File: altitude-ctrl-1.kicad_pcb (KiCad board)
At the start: 2 copper layers, 90 x 90 mm, 93 parts, among them J1 Conn_01x02, J10 Conn_01x02, J11 Conn_01x04, J2 Conn_01x02, J3 Conn_01x05, J4 TC2030, J5 Conn_01x04_Pin, J6 Conn_01x02, J7 Conn_01x05, J8 Conn_01x05, J9 Conn_01x02, SW1 SW_Push, SW2 SW_SPST, SW3 SW_Push, SW4 SW_SPST, SW5 SW_Push, U1 HT753-1, U2 ULN2003A, U3 LM73100, U4 LM73100, U5 MAX6675, U6 STM32F103C8Tx, U7 SN65HVD230, Y1 8M

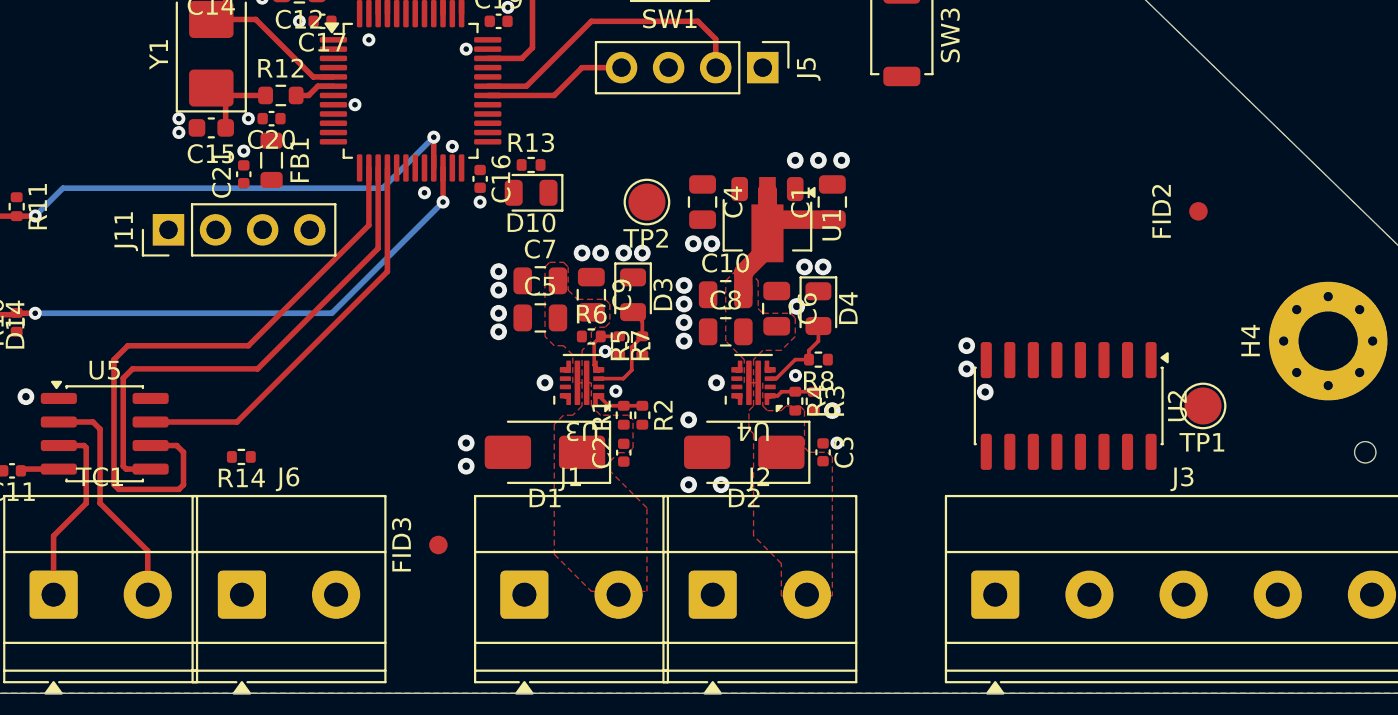
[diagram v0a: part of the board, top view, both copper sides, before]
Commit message: pcb: add relay driver routing
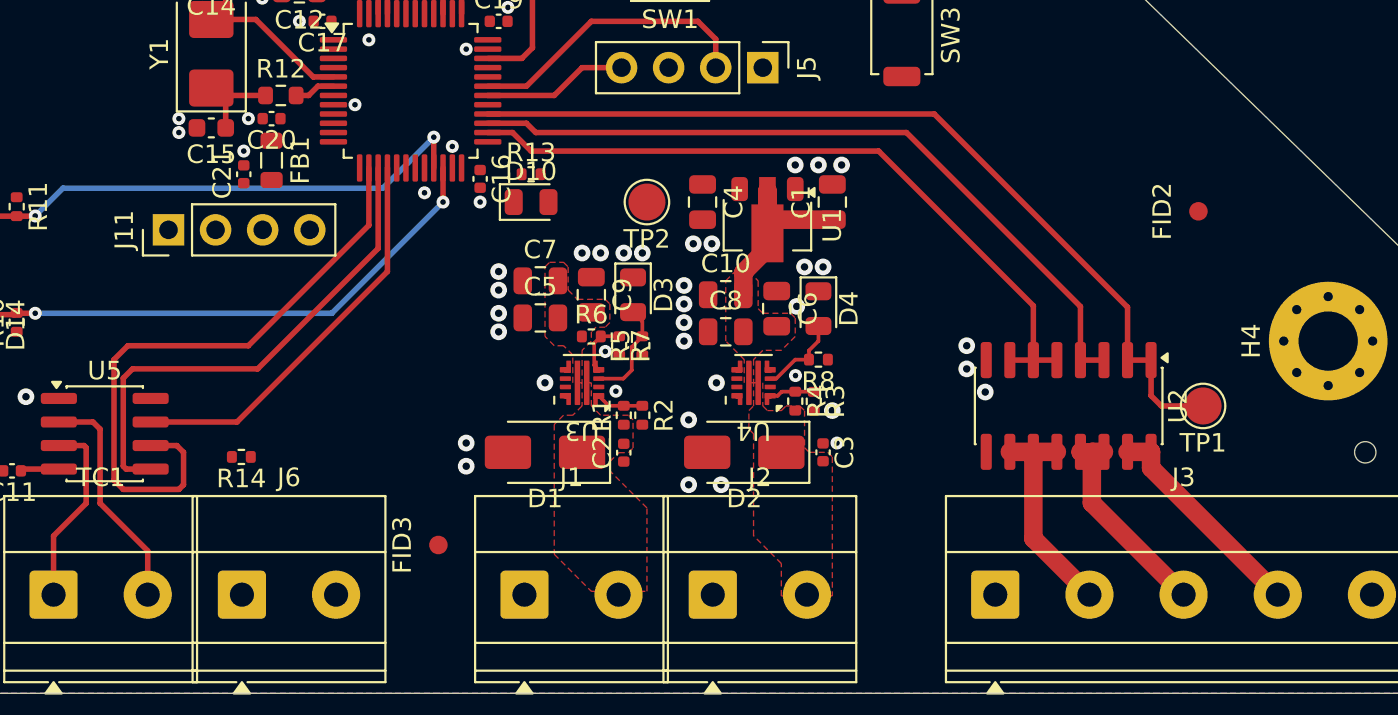
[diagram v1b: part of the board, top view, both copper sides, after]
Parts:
- moved D10 0.50 mm to (171.0, 92.5), turned to 0 degrees
- moved R13 0.50 mm to (171.0, 91.0)
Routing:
- net /PUMP: track 0.00 -> 47.9 mm
- net /RL1: track 0.00 -> 40.2 mm
- net /RL2: track 0.00 -> 38.8 mm
- net Net-(J3-Pin_4): track 0.00 -> 11.8 mm
- net Net-(J3-Pin_2): track 0.00 -> 11.5 mm
- net Net-(J3-Pin_3): track 0.00 -> 11.0 mm

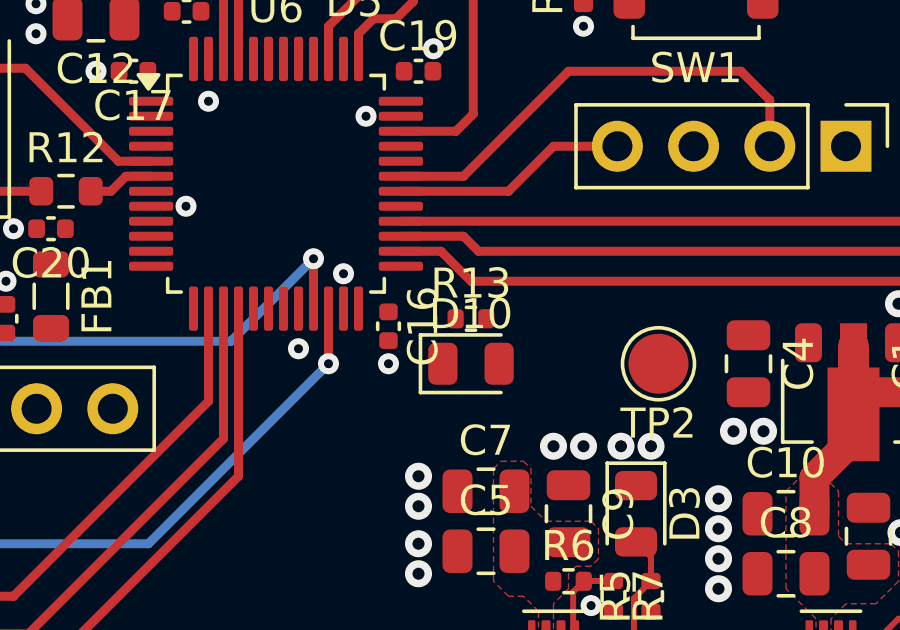
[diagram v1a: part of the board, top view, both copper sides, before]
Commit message: pcb: add can status led routing
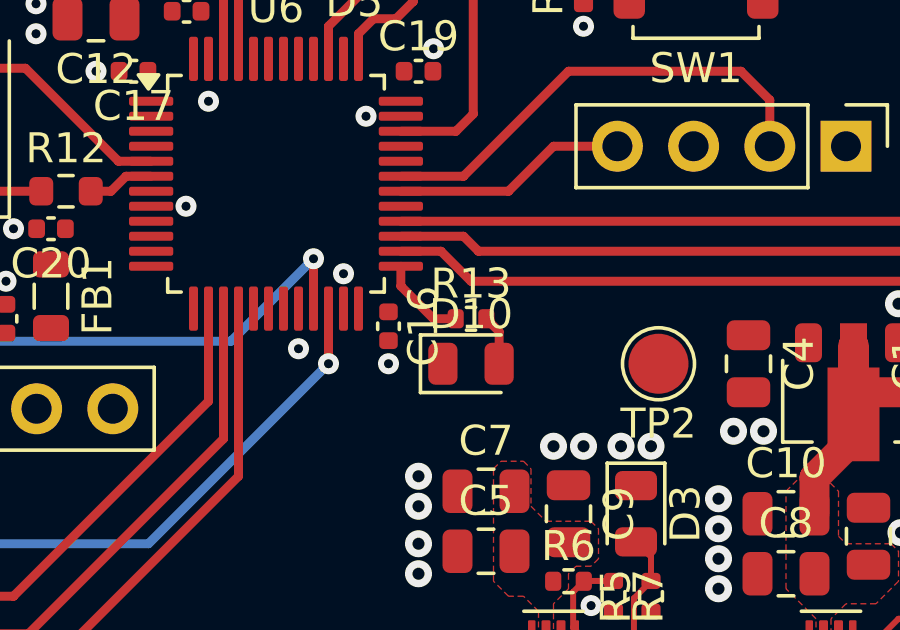
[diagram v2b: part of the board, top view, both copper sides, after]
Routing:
- net Net-(U6-PB12): track 0.00 -> 2.94 mm
- net Net-(D10-A): track 0.00 -> 1.68 mm
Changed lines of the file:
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@@
+	)
+	(segment
+		(start 171.9375 91.4275)
+		(end 171.51 91)
+		(width 0.3)
+		(layer "F.Cu")
+		(net "Net-(D10-A)")
+	)
+	(segment
+		(start 171.9375 92.5)
+		(end 171.9375 91.4275)
+		(width 0.3)
+		(layer "F.Cu")
+		(net "Net-(D10-A)")
 	)
 	(segment
@@
 		(net "Net-(TC1-+)")
 	)
+	(segment
+		(start 168.6625 89.9125)
+		(end 169.75 91)
+		(width 0.3)
+		(layer "F.Cu")
+		(net "Net-(U6-PB12)")
+	)
+	(segment
+		(start 169.75 91)
+		(end 170.49 91)
+		(width 0.3)
+		(layer "F.Cu")
+		(net "Net-(U6-PB12)")
+	)
+	(segment
+		(start 168.6625 89.25)
+		(end 168.6625 89.9125)
+		(width 0.3)
+		(layer "F.Cu")
+		(net "Net-(U6-PB12)")
+	)
 	(zone

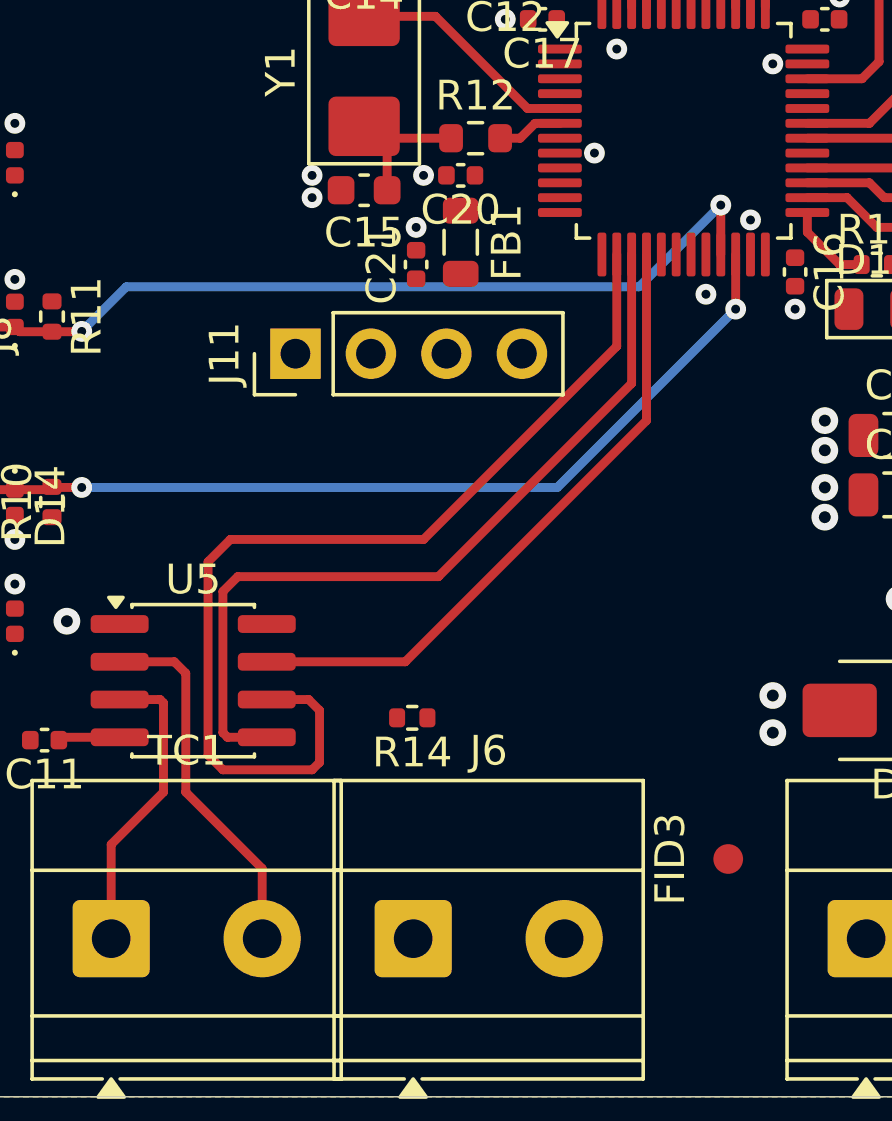
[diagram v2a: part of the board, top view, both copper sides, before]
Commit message: pcb: add gpio routing
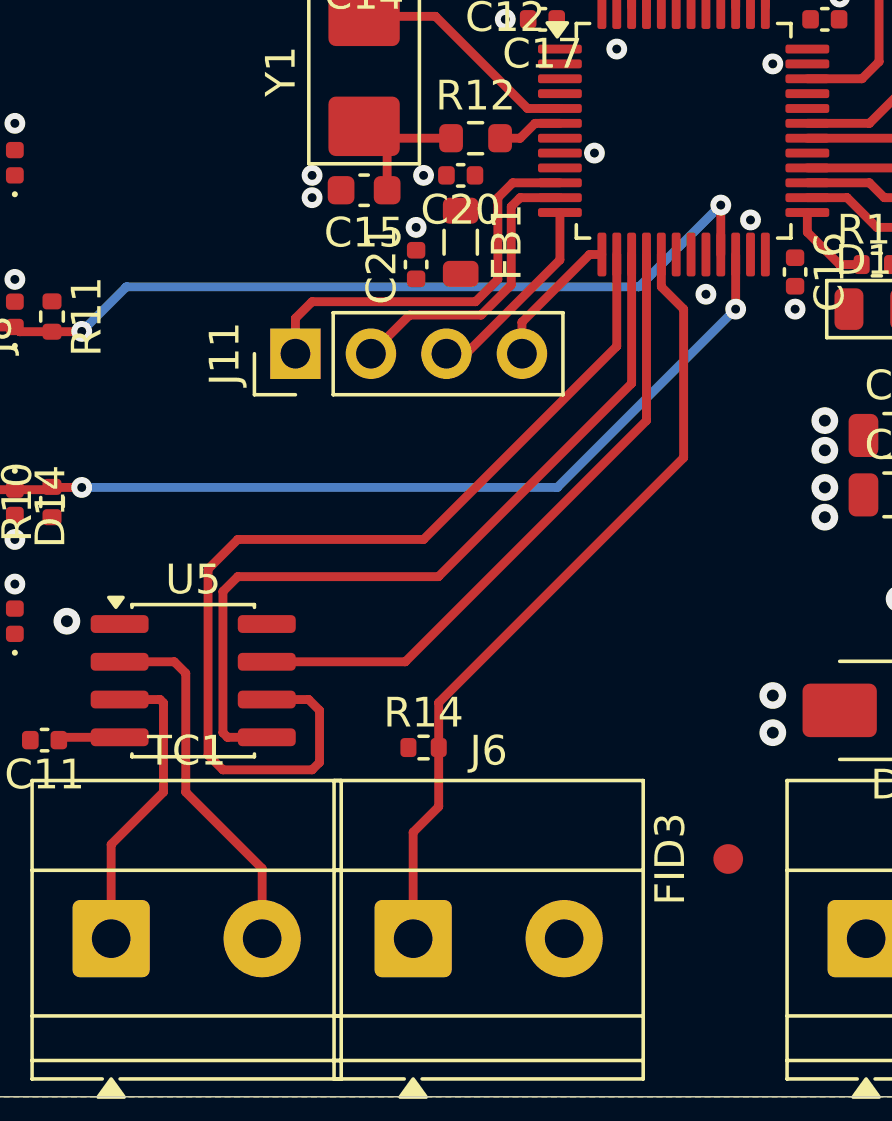
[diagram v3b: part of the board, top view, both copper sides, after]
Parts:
- moved R14 1.07 mm to (155.8, 107.2), turned to 0 degrees
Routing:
- net /PRES_SNS: track 0.00 -> 27.1 mm
- net Net-(J11-Pin_1): track 0.00 -> 13.6 mm
- net Net-(J11-Pin_2): track 0.00 -> 10.1 mm
- net Net-(J11-Pin_3): track 0.00 -> 6.72 mm
- net Net-(J11-Pin_4): track 0.00 -> 4.69 mm
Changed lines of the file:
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@@
 	(footprint "Resistor_SMD:R_0402_1005Metric"
 		(layer "F.Cu")
-		(at 155.37 106.25 180)
+		(at 155.75 107.25)
 		(descr "Resistor SMD 0402 (1005 Metric), square (rectangular) end terminal, IPC-7351 nominal, (Body size source: IPC-SM-782 page 72, https://www.pcb-3d.com/wordpress/wp-content/uploads/ipc-sm-782a_amendment_1_and_2.pdf)")
 		(tags "resistor")
@@
 		)
 		(property "Basic" "X"
-			(at 0 0 180)
+			(at 0 0 0)
 			(unlocked yes)
 			(layer "F.Fab")
@@
 		)
 		(property "JLCPCB Part #" "C705627"
-			(at 0 0 180)
+			(at 0 0 0)
 			(unlocked yes)
 			(layer "F.Fab")
@@
 		)
 		(property "Manufacturer" "YAGEO"
-			(at 0 0 180)
+			(at 0 0 0)
 			(unlocked yes)
 			(layer "F.Fab")
@@
 		)
 		(property "Manufacturer Part Number" "RT0402BRD07100RL"
-			(at 0 0 180)
+			(at 0 0 0)
 			(unlocked yes)
 			(layer "F.Fab")
@@
 		(duplicate_pad_numbers_are_jumpers no)
 		(fp_line
-			(start -0.153641 0.38)
-			(end 0.153641 0.38)
+			(start -0.153641 -0.38)
+			(end 0.153641 -0.38)
 			(stroke
 				(width 0.12)
@@
 		)
 		(fp_line
-			(start -0.153641 -0.38)
-			(end 0.153641 -0.38)
+			(start -0.153641 0.38)
+			(end 0.153641 0.38)
 			(stroke
 				(width 0.12)
@@
 		)
 		(pad "1" smd roundrect
-			(at -0.51 0 180)
+			(at -0.51 0)
 			(size 0.54 0.64)
 			(layers "F.Cu" "F.Mask" "F.Paste")
@@
 		)
 		(pad "2" smd roundrect
-			(at 0.51 0 180)
+			(at 0.51 0)
 			(size 0.54 0.64)
 			(layers "F.Cu" "F.Mask" "F.Paste")
@@
 	)
 	(segment
+		(start 156.26 105.74)
+		(end 156.26 107.25)
+		(width 0.3)
+		(layer "F.Cu")
+		(net "/PRES_SNS")
+	)
+	(segment
+		(start 164.5 92.5)
+		(end 164.5 97.5)
+		(width 0.3)
+		(layer "F.Cu")
+		(net "/PRES_SNS")
+	)
+	(segment
+		(start 163.75 90.6625)
+		(end 163.75 91.75)
+		(width 0.3)
+		(layer "F.Cu")
+		(net "/PRES_SNS")
+	)
+	(segment
+		(start 155.4 113.68)
+		(end 155.4 110.1)
+		(width 0.3)
+		(layer "F.Cu")
+		(net "/PRES_SNS")
+	)
+	(segment
+		(start 164.5 97.5)
+		(end 156.26 105.74)
+		(width 0.3)
+		(layer "F.Cu")
+		(net "/PRES_SNS")
+	)
+	(segment
+		(start 156.26 109.24)
+		(end 156.26 107.25)
+		(width 0.3)
+		(layer "F.Cu")
+		(net "/PRES_SNS")
+	)
+	(segment
+		(start 155.4 110.1)
+		(end 156.26 109.24)
+		(width 0.3)
+		(layer "F.Cu")
+		(net "/PRES_SNS")
+	)
+	(segment
+		(start 163.75 91.75)
+		(end 164.5 92.5)
+		(width 0.3)
+		(layer "F.Cu")
+		(net "/PRES_SNS")
+	)
+	(segment
 		(start 143.575 106.905)
 		(end 143.48 107)
@@
 	)
 	(segment
-		(start 152.25 107.75)
-		(end 152 108)
+		(start 152.25 106)
+		(end 152.25 107.75)
 		(width 0.3)
 		(layer "F.Cu")
@@
 	)
 	(segment
-		(start 149.25 100.25)
-		(end 155.750002 100.25)
+		(start 148.5 101.25)
+		(end 149.5 100.25)
 		(width 0.3)
 		(layer "F.Cu")
@@
 	)
 	(segment
-		(start 148.5 101)
-		(end 149.25 100.25)
+		(start 149 108)
+		(end 148.5 107.5)
 		(width 0.3)
 		(layer "F.Cu")
@@
 	)
 	(segment
-		(start 148.5 107.5)
-		(end 148.5 101)
+		(start 162.25 93.750002)
+		(end 162.25 90.6625)
 		(width 0.3)
 		(layer "F.Cu")
@@
 	)
 	(segment
-		(start 162.25 93.750002)
-		(end 162.25 90.6625)
+		(start 149.5 100.25)
+		(end 155.750002 100.25)
 		(width 0.3)
 		(layer "F.Cu")
@@
 	)
 	(segment
-		(start 152 108)
-		(end 149 108)
+		(start 155.750002 100.25)
+		(end 162.25 93.750002)
 		(width 0.3)
 		(layer "F.Cu")
@@
 	)
 	(segment
-		(start 149 108)
-		(end 148.5 107.5)
+		(start 152.25 107.75)
+		(end 152 108)
 		(width 0.3)
 		(layer "F.Cu")
@@
 	)
 	(segment
-		(start 150.475 105.635)
-		(end 151.885 105.635)
+		(start 152 108)
+		(end 149 108)
 		(width 0.3)
 		(layer "F.Cu")
@@
 	)
 	(segment
-		(start 155.750002 100.25)
-		(end 162.25 93.750002)
+		(start 148.5 107.5)
+		(end 148.5 101.25)
 		(width 0.3)
 		(layer "F.Cu")
@@
 	)
 	(segment
-		(start 152.25 106)
-		(end 152.25 107.75)
+		(start 150.475 105.635)
+		(end 151.885 105.635)
 		(width 0.3)
 		(layer "F.Cu")
@@
 	)
 	(segment
+		(start 157.5 92.25)
+		(end 152 92.25)
+		(width 0.3)
+		(layer "F.Cu")
+		(net "Net-(J11-Pin_1)")
+	)
+	(segment
+		(start 160.3375 88.25)
+		(end 158.75 88.25)
+		(width 0.3)
+		(layer "F.Cu")
+		(net "Net-(J11-Pin_1)")
+	)
+	(segment
+		(start 158.25 88.75)
+		(end 158.25 91.5)
+		(width 0.3)
+		(layer "F.Cu")
+		(net "Net-(J11-Pin_1)")
+	)
+	(segment
+		(start 151.44 92.81)
+		(end 151.44 94)
+		(width 0.3)
+		(layer "F.Cu")
+		(net "Net-(J11-Pin_1)")
+	)
+	(segment
+		(start 152 92.25)
+		(end 151.44 92.81)
+		(width 0.3)
+		(layer "F.Cu")
+		(net "Net-(J11-Pin_1)")
+	)
+	(segment
+		(start 158.25 91.5)
+		(end 157.5 92.25)
+		(width 0.3)
+		(layer "F.Cu")
+		(net "Net-(J11-Pin_1)")
+	)
+	(segment
+		(start 158.75 88.25)
+		(end 158.25 88.75)
+		(width 0.3)
+		(layer "F.Cu")
+		(net "Net-(J11-Pin_1)")
+	)
+	(segment
+		(start 159 88.75)
+		(end 160.3375 88.75)
+		(width 0.3)
+		(layer "F.Cu")
+		(net "Net-(J11-Pin_2)")
+	)
+	(segment
+		(start 157.686396 92.7)
+		(end 158.7 91.686396)
+		(width 0.3)
+		(layer "F.Cu")
+		(net "Net-(J11-Pin_2)")
+	)
+	(segment
+		(start 155.28 92.7)
+		(end 157.686396 92.7)
+		(width 0.3)
+		(layer "F.Cu")
+		(net "Net-(J11-Pin_2)")
+	)
+	(segment
+		(start 158.7 89.05)
+		(end 159 88.75)
+		(width 0.3)
+		(layer "F.Cu")
+		(net "Net-(J11-Pin_2)")
+	)
+	(segment
+		(start 158.7 91.686396)
+		(end 158.7 89.05)
+		(width 0.3)
+		(layer "F.Cu")
+		(net "Net-(J11-Pin_2)")
+	)
+	(segment
+		(start 153.98 94)
+		(end 155.28 92.7)
+		(width 0.3)
+		(layer "F.Cu")
+		(net "Net-(J11-Pin_2)")
+	)
+	(segment
+		(start 157.181259 94)
+		(end 156.52 94)
+		(width 0.3)
+		(layer "F.Cu")
+		(net "Net-(J11-Pin_3)")
+	)
+	(segment
+		(start 160.3375 90.843759)
+		(end 157.181259 94)
+		(width 0.3)
+		(layer "F.Cu")
+		(net "Net-(J11-Pin_3)")
+	)
+	(segment
+		(start 160.3375 89.25)
+		(end 160.3375 90.843759)
+		(width 0.3)
+		(layer "F.Cu")
+		(net "Net-(J11-Pin_3)")
+	)
+	(segment
+		(start 161.3375 90.6625)
+		(end 159.06 92.94)
+		(width 0.3)
+		(layer "F.Cu")
+		(net "Net-(J11-Pin_4)")
+	)
+	(segment
+		(start 161.75 90.6625)
+		(end 161.3375 90.6625)
+		(width 0.3)
+		(layer "F.Cu")
+		(net "Net-(J11-Pin_4)")
+	)
+	(segment
+		(start 159.06 92.94)
+		(end 159.06 94)
+		(width 0.3)
+		(layer "F.Cu")
+		(net "Net-(J11-Pin_4)")
+	)
+	(segment
